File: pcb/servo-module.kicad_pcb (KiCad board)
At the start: 4 copper layers, 50 x 50 mm, 20 parts, among them J1 AVR-UPDI-6, J2 QWICC, J3 Power, U2 ATtiny1616-M

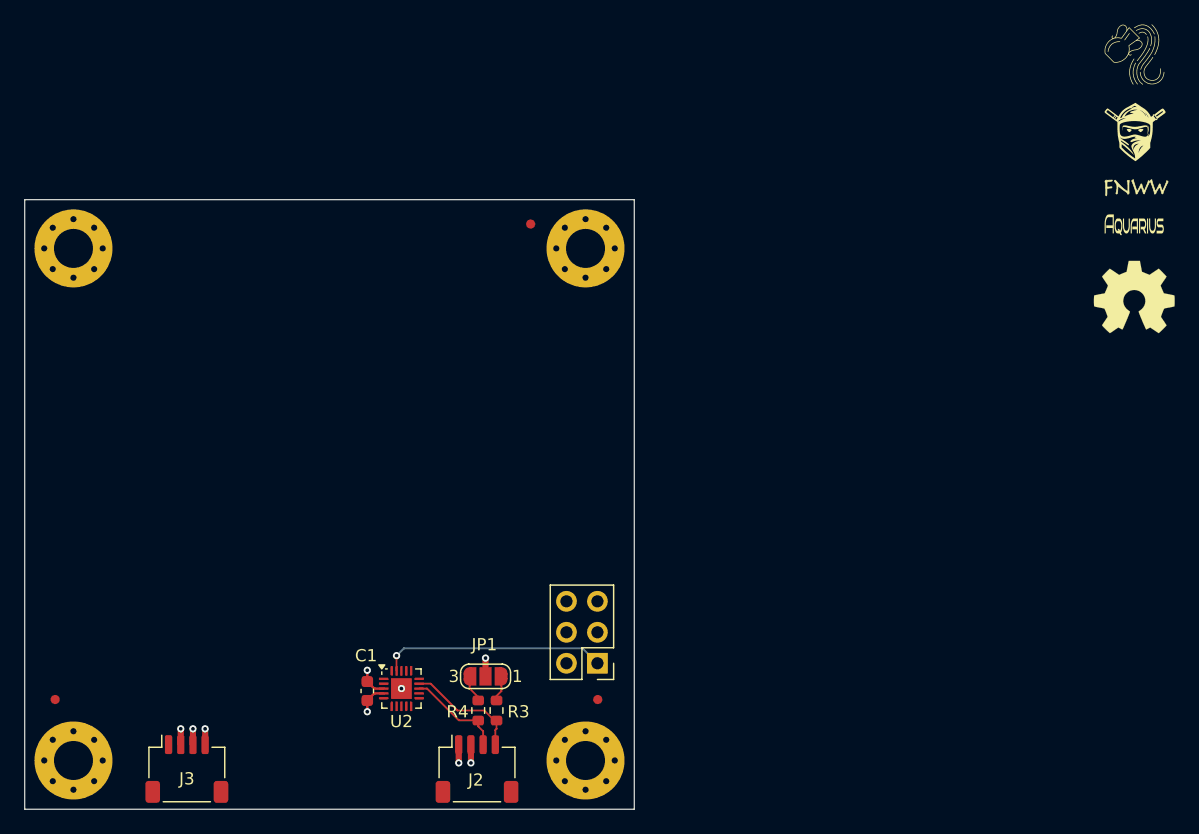
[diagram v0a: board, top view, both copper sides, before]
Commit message: added connectors
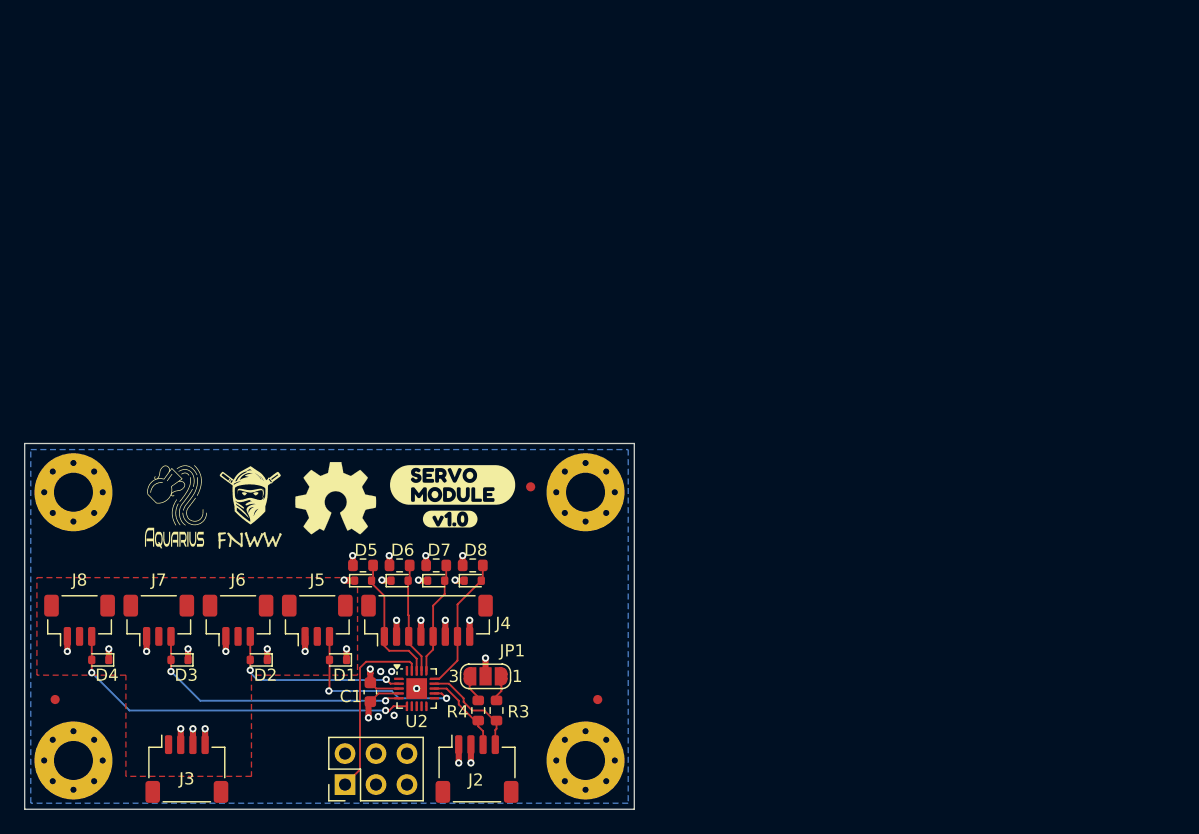
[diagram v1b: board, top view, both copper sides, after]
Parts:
- added D1: PESD5V0S1BB, CRGM Passive:D_SOD-523, F.Cu at (75.7, 152.8)
- added D2: PESD5V0S1BB, CRGM Passive:D_SOD-523, F.Cu at (69.2, 152.8)
- added D3: PESD5V0S1BB, CRGM Passive:D_SOD-523, F.Cu at (62.7, 152.8)
- added D4: PESD5V0S1BB, CRGM Passive:D_SOD-523, F.Cu at (56.2, 152.8)
- added D5: PESD5V0S1BB, CRGM Passive:D_SOD-523, F.Cu at (77.8, 146.2)
- added D6: PESD5V0S1BB, CRGM Passive:D_SOD-523, F.Cu at (80.8, 146.2)
- added D7: PESD5V0S1BB, CRGM Passive:D_SOD-523, F.Cu at (83.8, 146.2)
- added D8: PESD5V0S1BB, CRGM Passive:D_SOD-523, F.Cu at (86.8, 146.2)
- added J4: ~, Connector_JST:JST_SH_BM08B-SRSS-TB_1x08-1MP_P1.00mm_Vertical, F.Cu at (83.0, 149.5)
- added J5: ~, Connector_JST:JST_SH_BM03B-SRSS-TB_1x03-1MP_P1.00mm_Vertical, F.Cu at (74.0, 149.5)
- added J6: ~, Connector_JST:JST_SH_BM03B-SRSS-TB_1x03-1MP_P1.00mm_Vertical, F.Cu at (67.5, 149.5)
- added J7: ~, Connector_JST:JST_SH_BM03B-SRSS-TB_1x03-1MP_P1.00mm_Vertical, F.Cu at (61.0, 149.5)
- added J8: ~, Connector_JST:JST_SH_BM03B-SRSS-TB_1x03-1MP_P1.00mm_Vertical, F.Cu at (54.5, 149.5)
- added R5: 10K, Resistor_SMD:R_0603_1608Metric, F.Cu at (77.8, 145.0)
- added R6: 10K, Resistor_SMD:R_0603_1608Metric, F.Cu at (80.8, 145.0)
- added R7: 10K, Resistor_SMD:R_0603_1608Metric, F.Cu at (83.8, 145.0)
- added R8: 10K, Resistor_SMD:R_0603_1608Metric, F.Cu at (86.8, 145.0)
- added kibuzzard-67E4BAC2: G***, kibuzzard-67E4BAC2, F.Cu at (85.1, 138.4)
- added kibuzzard-67E4BADC: G***, kibuzzard-67E4BADC, F.Cu at (84.9, 141.2)
- moved LOGO1 86.4 mm to (62.4, 142.0)
- moved LOGO2 82.8 mm to (62.4, 143.8)
- moved LOGO3 78.5 mm to (68.5, 141.9)
- moved LOGO4 78.3 mm to (68.5, 143.9)
- moved LOGO5 67.5 mm to (75.5, 139.5)
- moved J1 23.0 mm to (76.3, 163.0), turned to 90 degrees
- moved FID3 21.6 mm to (91.5, 138.6)
- moved H3 20.0 mm to (96.0, 139.0)
- moved H4 20.0 mm to (54.0, 139.0)
- moved U2 1.25 mm to (82.2, 155.1)
- moved C1 0.27 mm to (78.3, 155.4)
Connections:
- U2 pad 12: unconnected-(U2-PB2-Pad12) -> /PWM1
- U2 pad 15: /RELAY_CTRL -> /IN1
- U2 pad 16: unconnected-(U2-PC1-Pad16) -> /IN2
- U2 pad 17: unconnected-(U2-PC2-Pad17) -> /IN3
- U2 pad 18: unconnected-(U2-PC3-Pad18) -> /IN4
- U2 pad 2: unconnected-(U2-PA3-Pad2) -> /PWM2
- U2 pad 5: unconnected-(U2-PA4-Pad5) -> /PWM3
- U2 pad 6: unconnected-(U2-PA5-Pad6) -> /PWM4
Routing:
- net /PWM4: track 0.00 -> 30.3 mm, vias 0 -> 2
- net /PWM3: track 0.00 -> 22.7 mm, vias 0 -> 2
- net GND: track 6.61 -> 24.8 mm, vias 5 -> 25
- net /PWM2: track 0.00 -> 15.6 mm, vias 0 -> 2
- net /PWM1: track 0.00 -> 15.6 mm, vias 0 -> 2
- net /IN1: track 0.00 -> 11.2 mm
- net /IN4: track 0.00 -> 11.2 mm
- net /IN2: track 0.00 -> 9.32 mm
- net /IN3: track 0.00 -> 9.16 mm
- net +3.3V: track 6.81 -> 11.5 mm, vias 4 -> 8
- net /UPDI: track 18.5 -> 15.7 mm, vias 1 -> 0
- net /SCL: track 9.65 -> 8.58 mm
- net /SDA: track 8.08 -> 7.00 mm
- added copper zone on In2.Cu, net +3.3V
- added copper zone on F.Cu, net +5V
- added copper zone on B.Cu, net GND
- added copper zone on In1.Cu, net GND
- removed copper zone on In1.Cu, net +3.3V
- removed copper zone on In2.Cu, net GND
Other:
- board size 50 x 50 mm -> 50 x 30 mm

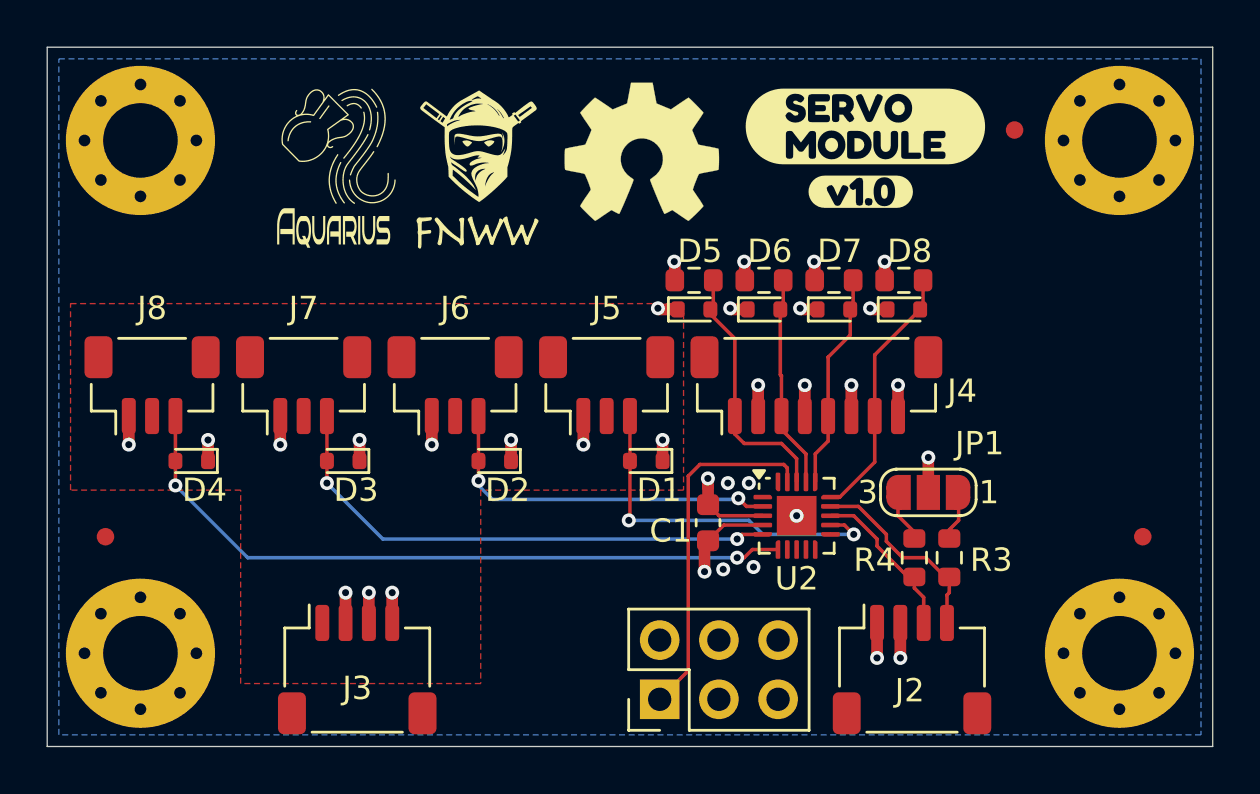
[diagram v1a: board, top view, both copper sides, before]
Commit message: Added additional suppliers and changed some footprints for DRC
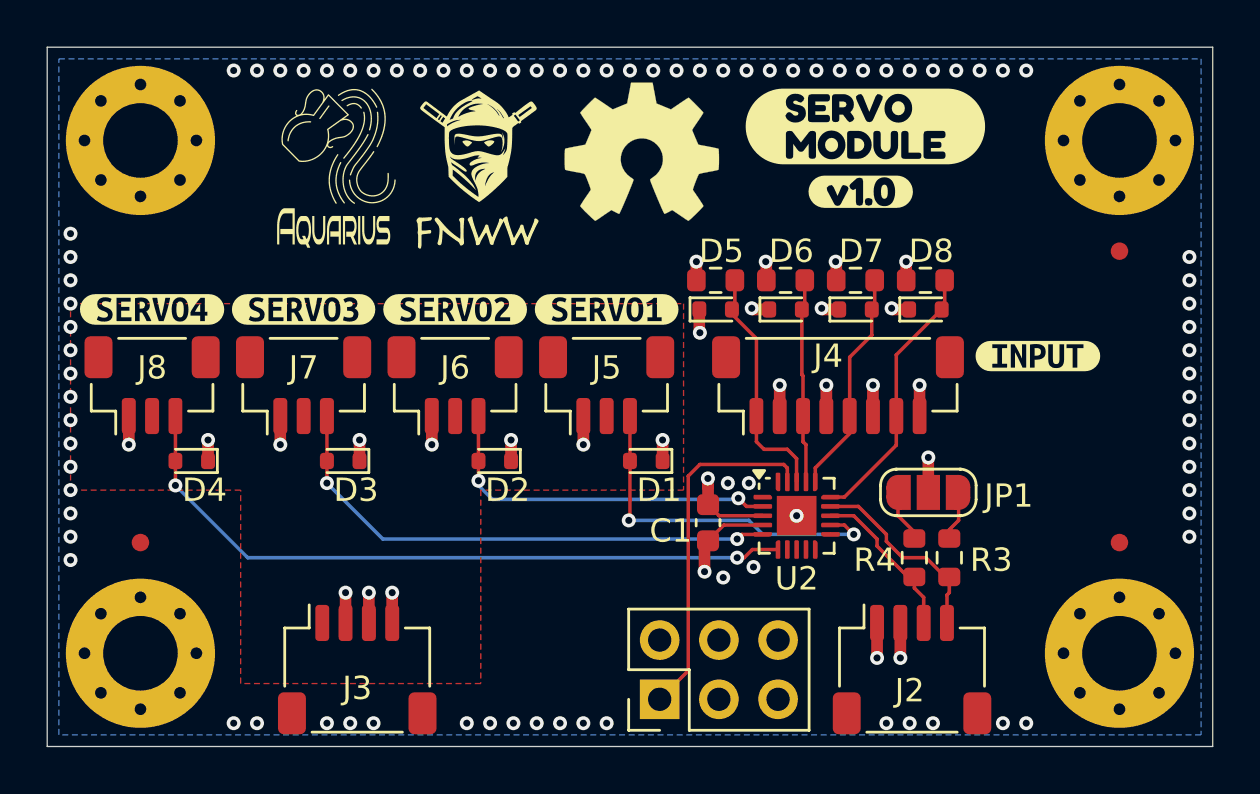
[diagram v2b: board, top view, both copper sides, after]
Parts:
- added kibuzzard-67E9F1A1: G***, kibuzzard-67E9F1A1, F.Cu at (67.5, 146.2)
- added kibuzzard-67E9F1AC: G***, kibuzzard-67E9F1AC, F.Cu at (74.0, 146.2)
- added kibuzzard-67E9F1C4: G***, kibuzzard-67E9F1C4, F.Cu at (61.0, 146.2)
- added kibuzzard-67E9F26B: G***, kibuzzard-67E9F26B, F.Cu at (54.5, 146.2)
- added kibuzzard-67E9F303: G***, kibuzzard-67E9F303, F.Cu at (92.5, 148.2)
- J4: value ~ -> INPUT
- J5: value ~ -> PWM1
- J6: value ~ -> PWM2
- J7: value ~ -> PWM3
- J8: value ~ -> PWM4
- U2: value ATtiny1616-M -> ATTINY1616MNR
- moved FID3 6.87 mm to (96.0, 143.8)
- moved FID1 1.52 mm to (54.0, 156.2)
- moved FID2 1.03 mm to (96.0, 156.2)
- moved D5 0.92 mm to (78.7, 146.2)
- moved D6 0.92 mm to (81.7, 146.2)
- moved D7 0.92 mm to (84.7, 146.2)
- moved D8 0.92 mm to (87.7, 146.2)
- moved J4 0.92 mm to (83.9, 149.5)
- moved R5 0.92 mm to (78.7, 145.0)
- moved R6 0.92 mm to (81.7, 145.0)
- moved R7 0.92 mm to (84.7, 145.0)
- moved R8 0.92 mm to (87.7, 145.0)
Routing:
- net /IN4: track 11.2 -> 10.4 mm
- net /IN1: track 11.2 -> 11.7 mm
- net GND: track 24.8 -> 24.9 mm, vias 25 -> 105

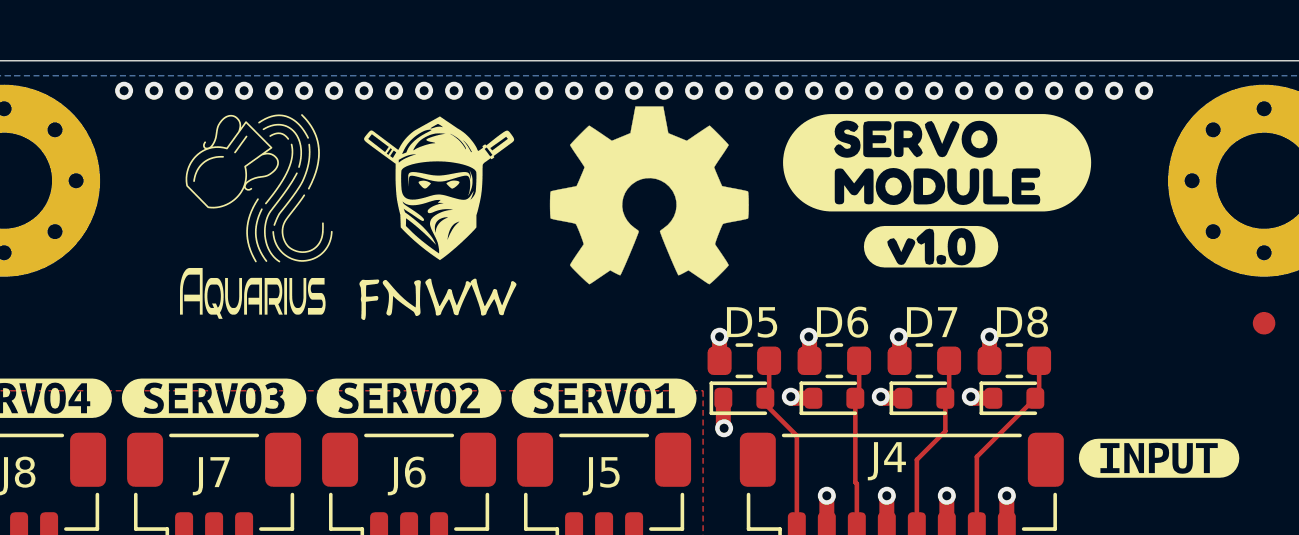
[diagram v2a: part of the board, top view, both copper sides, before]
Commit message: Updated silkscreen
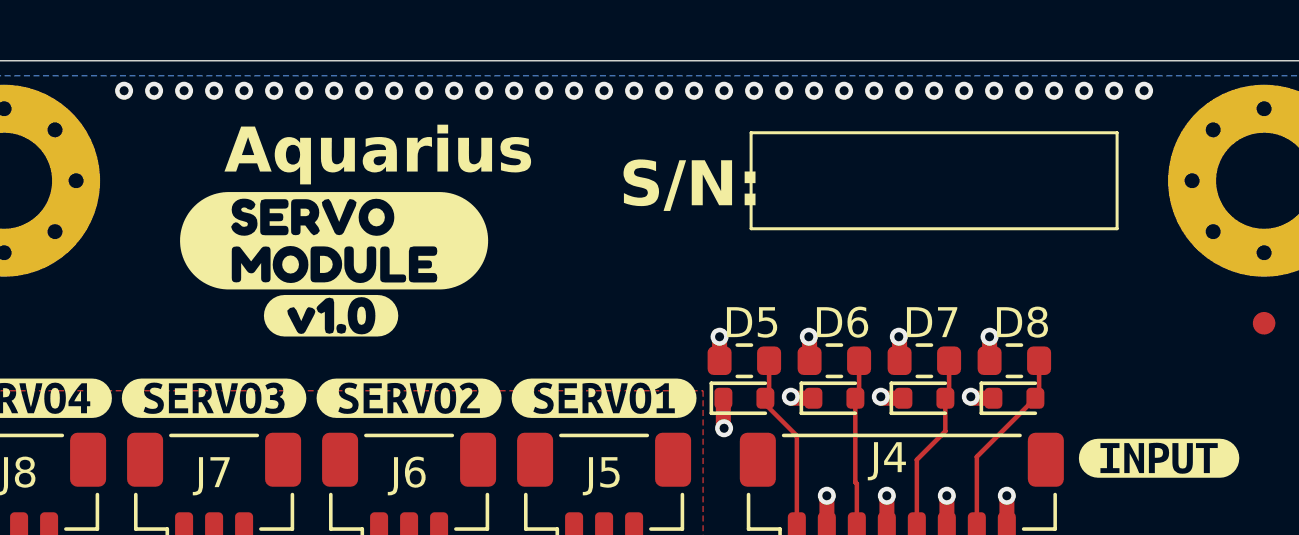
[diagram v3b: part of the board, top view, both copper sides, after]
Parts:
- removed LOGO2: ~, CRGM Logos:Aquarius Name 2mmx5mm
- removed LOGO4: ~, CRGM Logos:FNWW Name 2mmx5mm
- added kibuzzard-67F88258: G***, kibuzzard-67F88258, B.Cu at (75.1, 152.6)
- added kibuzzard-67F8826B: G***, kibuzzard-67F8826B, B.Cu at (75.0, 156.6)
- LOGO1: footprint CRGM Logos:Aquarius Logo 5mm -> CRGM Logos:Aquarius Logo 10mm; moved to B.Cu
- LOGO3: footprint CRGM Logos:FNWW Face 5mm -> CRGM Logos:FNWW Face 10mm; moved to B.Cu
- LOGO5: footprint Symbol:OSHW-Symbol_6.7x6mm_SilkScreen -> Symbol:OSHW-Logo_5.7x6mm_SilkScreen; moved to B.Cu
- moved LOGO5 23.7 mm to (95.0, 153.0), turned to 180 degrees
- moved kibuzzard-67E4BAC2 20.3 mm to (65.0, 141.0)
- moved kibuzzard-67E4BADC 20.1 mm to (64.9, 143.5)
- moved LOGO3 14.0 mm to (81.5, 146.9), turned to 180 degrees
- moved LOGO1 9.99 mm to (70.7, 147.5), turned to 180 degrees
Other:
- board text added: "Aquarius"
- board text added: "FNWW"
- board text added: "S/N:"
